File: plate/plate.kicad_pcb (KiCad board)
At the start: 2 copper layers, 157.6 x 110.6 mm, 8 parts, among them J1 Conn_01x06, J2 Conn_01x06, J3 Conn_01x06, J4 Conn_01x06, J5 Conn_01x06, J6 Conn_01x06

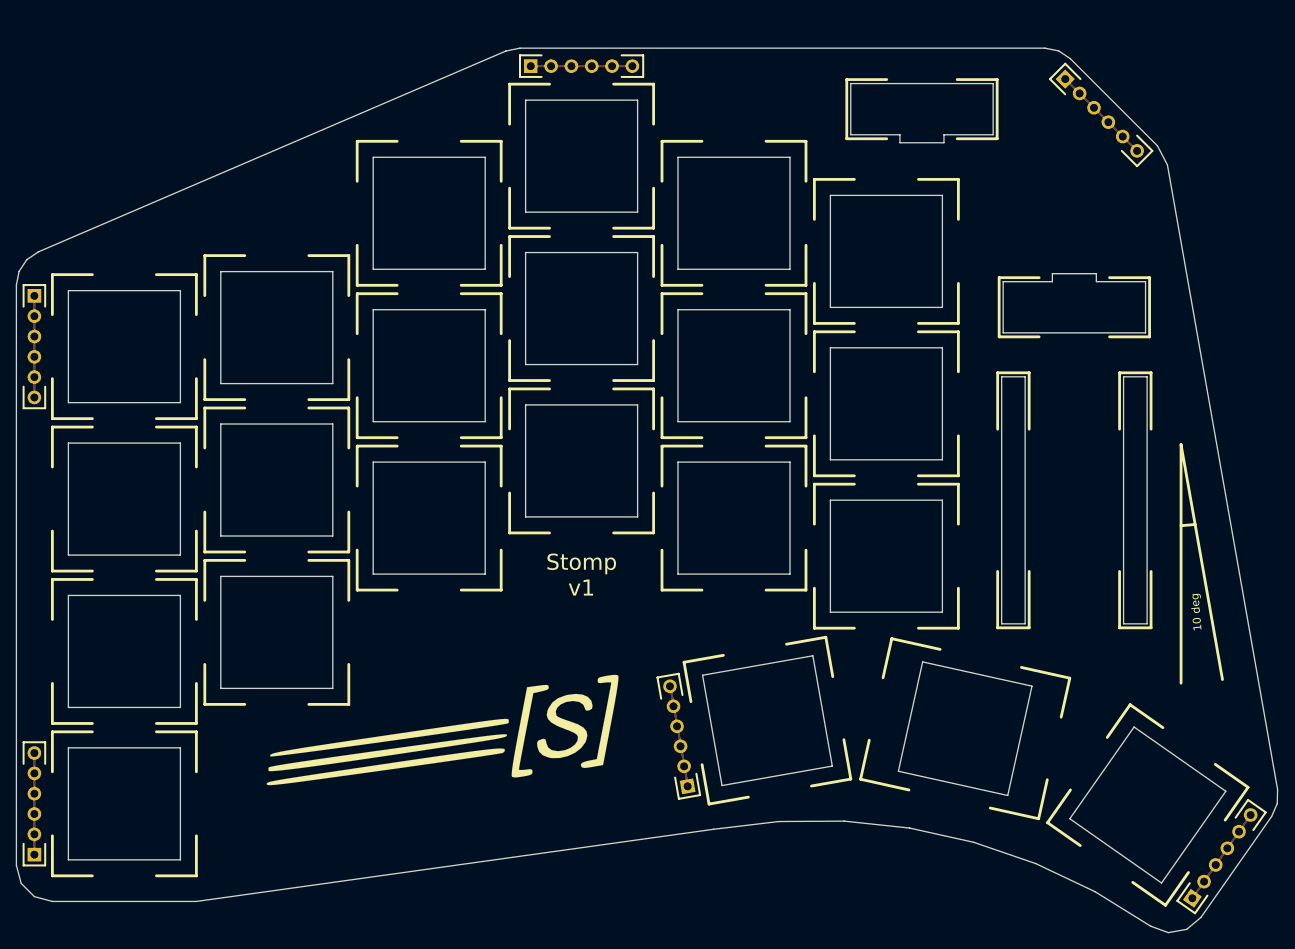
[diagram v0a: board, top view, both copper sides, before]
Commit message: Change board outline
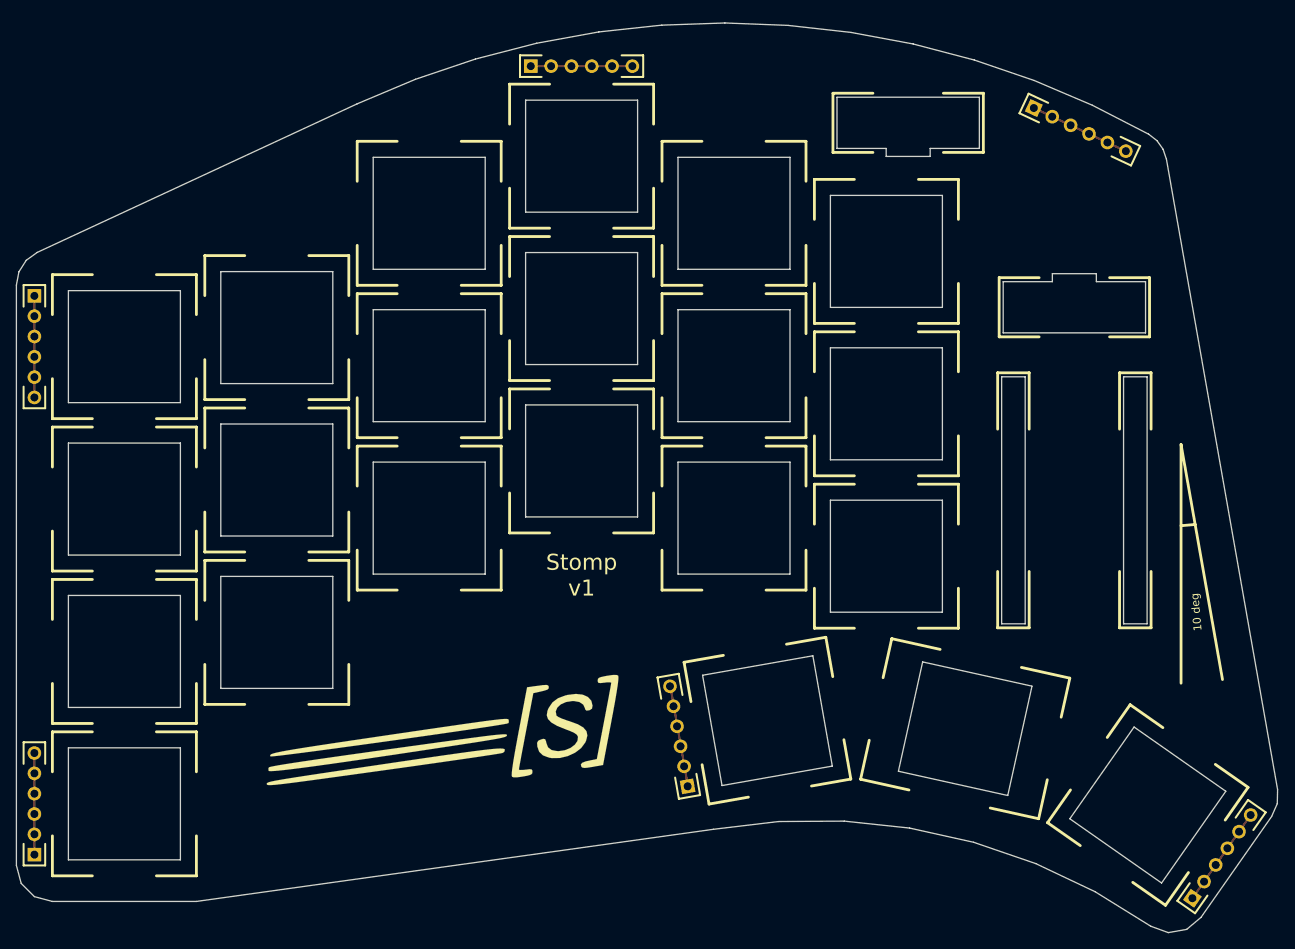
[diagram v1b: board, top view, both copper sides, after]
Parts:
- moved J6 5.34 mm to (8.90, -65.5), turned to 64.9 degrees
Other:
- board size 157.6 x 110.6 mm -> 157.6 x 113.7 mm

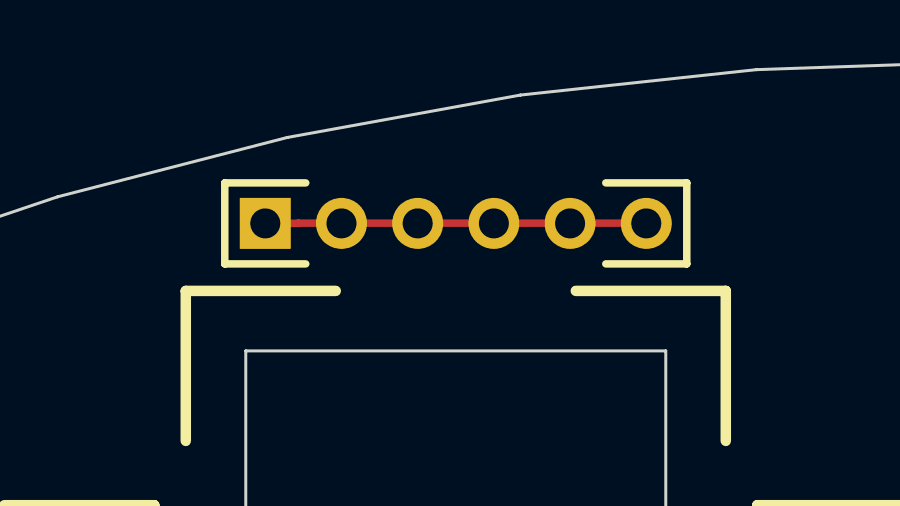
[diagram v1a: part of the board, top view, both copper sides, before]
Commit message: Fix one header
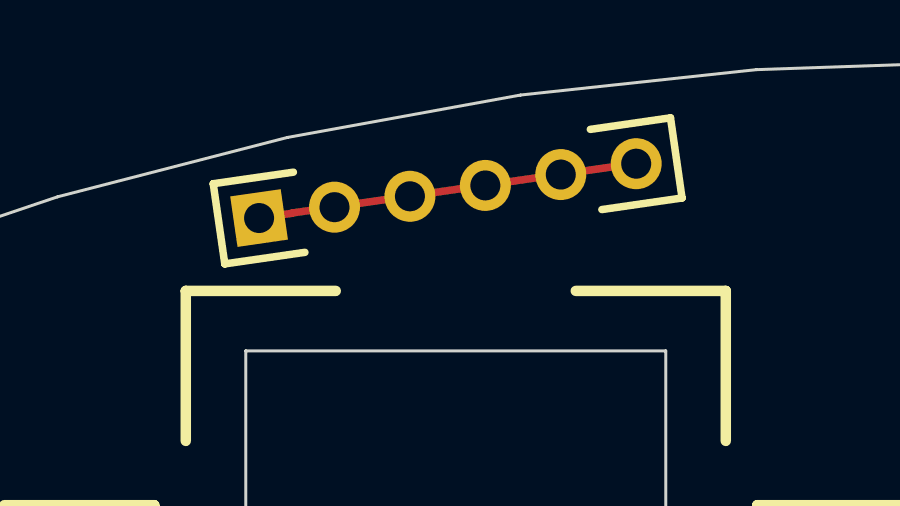
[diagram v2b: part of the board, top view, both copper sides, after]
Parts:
- moved J1 0.27 mm to (-54.2, -71.0), turned to 98.2 degrees
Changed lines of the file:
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@@
     (thickness 1.6)
     (drawings 562)
-    (tracks 10)
+    (tracks 9)
     (zones 0)
     (modules 8)
@@
   )
   (module keyboard-parts:header_1x06_2.54mm (layer F.Cu)
-    (at -53.975 -70.78125 90)
-    (fp_text reference J1 (at 0 -2.33 90) (layer F.SilkS) hide
-      (effects (font (size 1 1) (thickness 0.15)))
-    )
-    (fp_text value Conn_01x06 (at 0 15.24 90) (layer F.Fab)
-      (effects (font (size 1 1) (thickness 0.15)))
-    )
-    (fp_text user %R (at 0 -2.33 90) (layer B.SilkS) hide
+    (at -54.181351 -70.959997 98.2)
+    (fp_text reference J1 (at 0 -2.33 98.2) (layer F.SilkS) hide
+      (effects (font (size 1 1) (thickness 0.15)))
+    )
+    (fp_text value Conn_01x06 (at 0 15.24 98.2) (layer F.Fab)
+      (effects (font (size 1 1) (thickness 0.15)))
+    )
+    (fp_text user %R (at 0 -2.33 98.2) (layer B.SilkS) hide
       (effects (font (size 1 1) (thickness 0.15)) (justify mirror))
     )
@@
     (fp_line (start 1.35 14.05) (end 1.35 11.35) (layer B.SilkS) (width 0.25))
     (fp_line (start -1.35 14.05) (end -1.35 11.35) (layer B.SilkS) (width 0.25))
-    (fp_text user %R (at 0 5.08) (layer F.Fab)
+    (fp_text user %R (at 0 5.08 8.2) (layer F.Fab)
       (effects (font (size 1 1) (thickness 0.15)))
     )
@@
     (fp_line (start -1.35 14.05) (end -1.35 11.35) (layer F.SilkS) (width 0.25))
     (fp_line (start -1.35 -1.35) (end 1.35 -1.35) (layer F.SilkS) (width 0.25))
-    (pad 6 thru_hole oval (at 0 12.7 90) (size 1.7 1.7) (drill 1) (layers *.Cu *.Mask)
+    (pad 6 thru_hole oval (at 0 12.7 98.2) (size 1.7 1.7) (drill 1) (layers *.Cu *.Mask)
       (net 1 "Net-(J1-Pad1)"))
-    (pad 4 thru_hole oval (at 0 7.62 90) (size 1.7 1.7) (drill 1) (layers *.Cu *.Mask)
+    (pad 4 thru_hole oval (at 0 7.62 98.2) (size 1.7 1.7) (drill 1) (layers *.Cu *.Mask)
       (net 1 "Net-(J1-Pad1)"))
-    (pad 3 thru_hole oval (at 0 5.08 90) (size 1.7 1.7) (drill 1) (layers *.Cu *.Mask)
+    (pad 3 thru_hole oval (at 0 5.08 98.2) (size 1.7 1.7) (drill 1) (layers *.Cu *.Mask)
       (net 1 "Net-(J1-Pad1)"))
-    (pad 2 thru_hole oval (at 0 2.54 90) (size 1.7 1.7) (drill 1) (layers *.Cu *.Mask)
+    (pad 2 thru_hole oval (at 0 2.54 98.2) (size 1.7 1.7) (drill 1) (layers *.Cu *.Mask)
       (net 1 "Net-(J1-Pad1)"))
-    (pad 1 thru_hole rect (at 0 0 90) (size 1.7 1.7) (drill 1) (layers *.Cu *.Mask)
+    (pad 1 thru_hole rect (at 0 0 98.2) (size 1.7 1.7) (drill 1) (layers *.Cu *.Mask)
       (net 1 "Net-(J1-Pad1)"))
-    (pad 5 thru_hole oval (at 0 10.16 90) (size 1.7 1.7) (drill 1) (layers *.Cu *.Mask)
+    (pad 5 thru_hole oval (at 0 10.16 98.2) (size 1.7 1.7) (drill 1) (layers *.Cu *.Mask)
       (net 1 "Net-(J1-Pad1)"))
     (model ${KISYS3DMOD}/Connector_PinHeader_2.54mm.3dshapes/PinHeader_1x06_P2.54mm_Vertical.wrl
@@
     (effects (font (size 1 1) (thickness 0.2)))
   )
-  (segment (start -52.875 -70.78125) (end -52.86645 -70.7898) (width 0.25) (layer F.Cu) (net 1))
-  (segment (start -53.975 -70.78125) (end -52.875 -70.78125) (width 0.25) (layer F.Cu) (net 1))
-  (segment (start -52.86645 -70.7898) (end -41.275 -70.7898) (width 0.25) (layer F.Cu) (net 1))
+  (segment (start -54.181351 -70.959997) (end -53.092597 -71.116889) (width 0.25) (layer F.Cu) (net 1))
+  (segment (start -53.085354 -71.126571) (end -41.612412 -72.779847) (width 0.25) (layer F.Cu) (net 1))
   (segment (start -116.025 -42.06875) (end -116.025 -29.425) (width 0.25) (layer F.Cu) (net 2))
   (segment (start -116.025 27.781248) (end -116.025 15.125) (width 0.25) (layer F.Cu) (net 3))

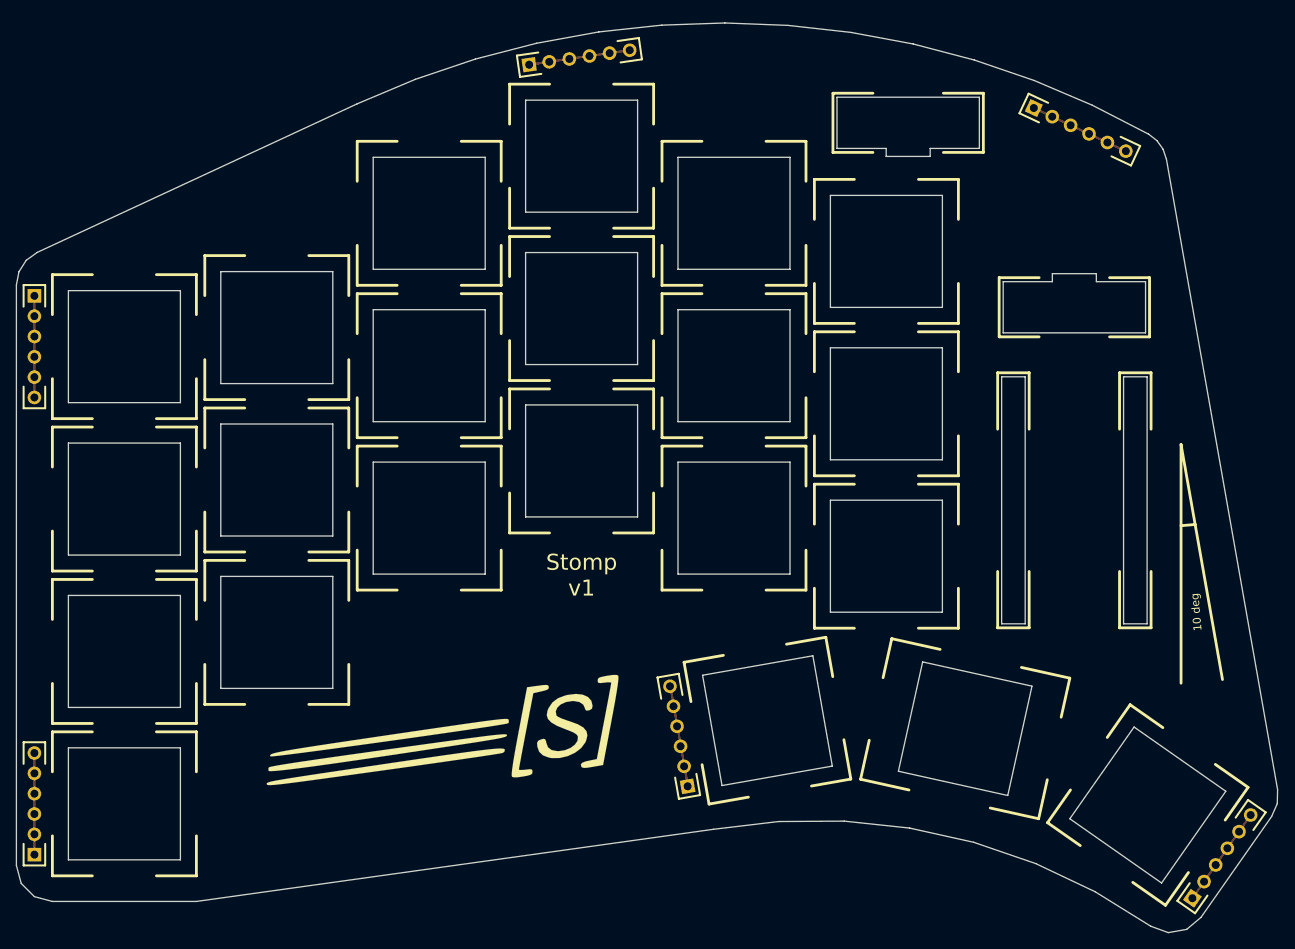
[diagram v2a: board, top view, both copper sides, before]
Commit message: Finish refinement of board outline
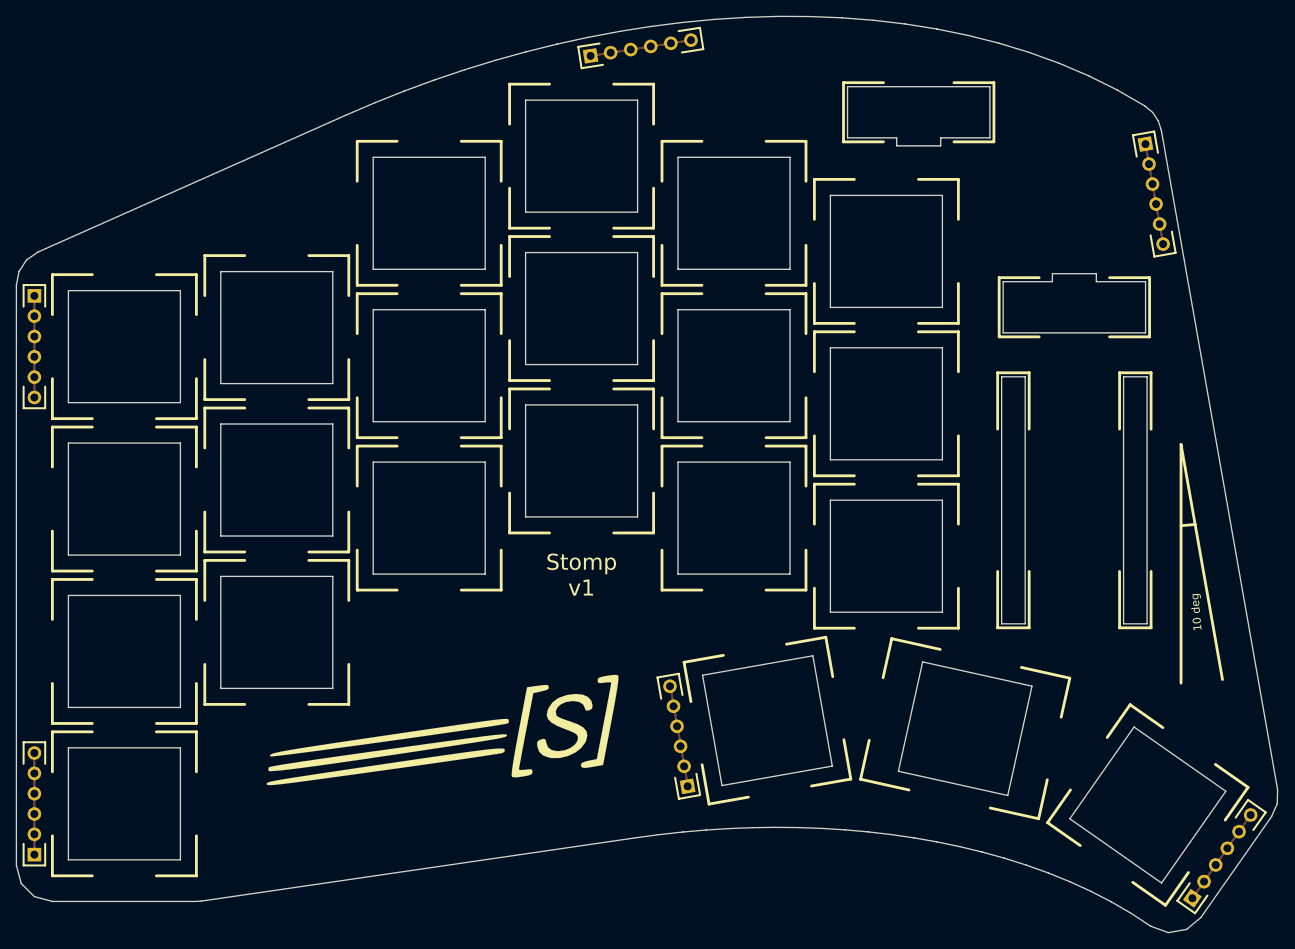
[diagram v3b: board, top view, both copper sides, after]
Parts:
- moved J6 14.7 mm to (22.9, -61.0), turned to 10 degrees
- moved J1 7.76 mm to (-46.5, -72.1), turned to 98.9 degrees
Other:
- board size 157.6 x 113.7 mm -> 157.6 x 114.5 mm

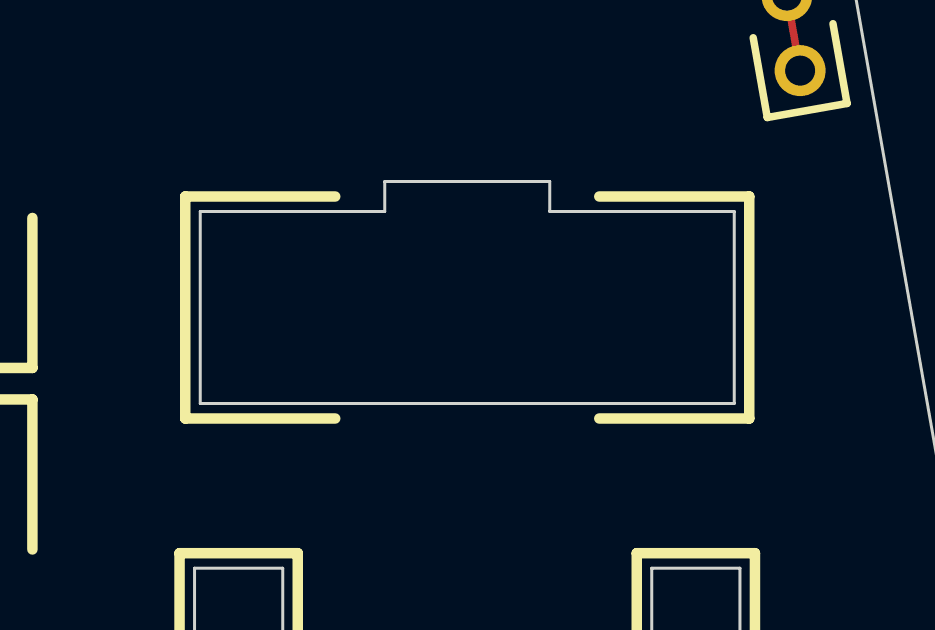
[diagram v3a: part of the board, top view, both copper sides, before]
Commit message: Slight reposition and reroute of inter-pcb-header
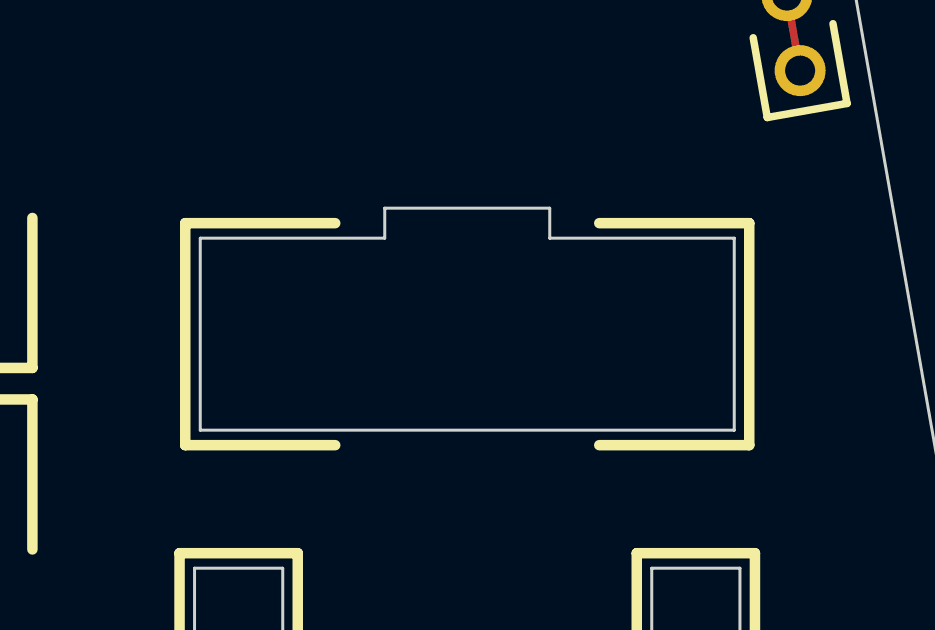
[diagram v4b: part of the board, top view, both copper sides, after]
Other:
- outline, holes or cut-outs redrawn

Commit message: Use single IDC header and prep outline for magnets
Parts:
- J1, J2, J3, J4, J5, J6: footprint keyboard-parts:header_1x06_2.54mm -> keyboard-parts:header_sym_1x06_2.54mm
- moved J1 4.96 mm to (-51.3, -71.0), turned to 100.9 degrees
- moved J6 2.82 mm to (21.0, -63.1), turned to 242.4 degrees
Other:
- outline, holes or cut-outs redrawn
